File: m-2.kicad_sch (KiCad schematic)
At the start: 46 parts, among them J5 1-2199230-6, J6 1-2199230-6, M1 M2_2280, M2 M2_2280, P1 2199230-6

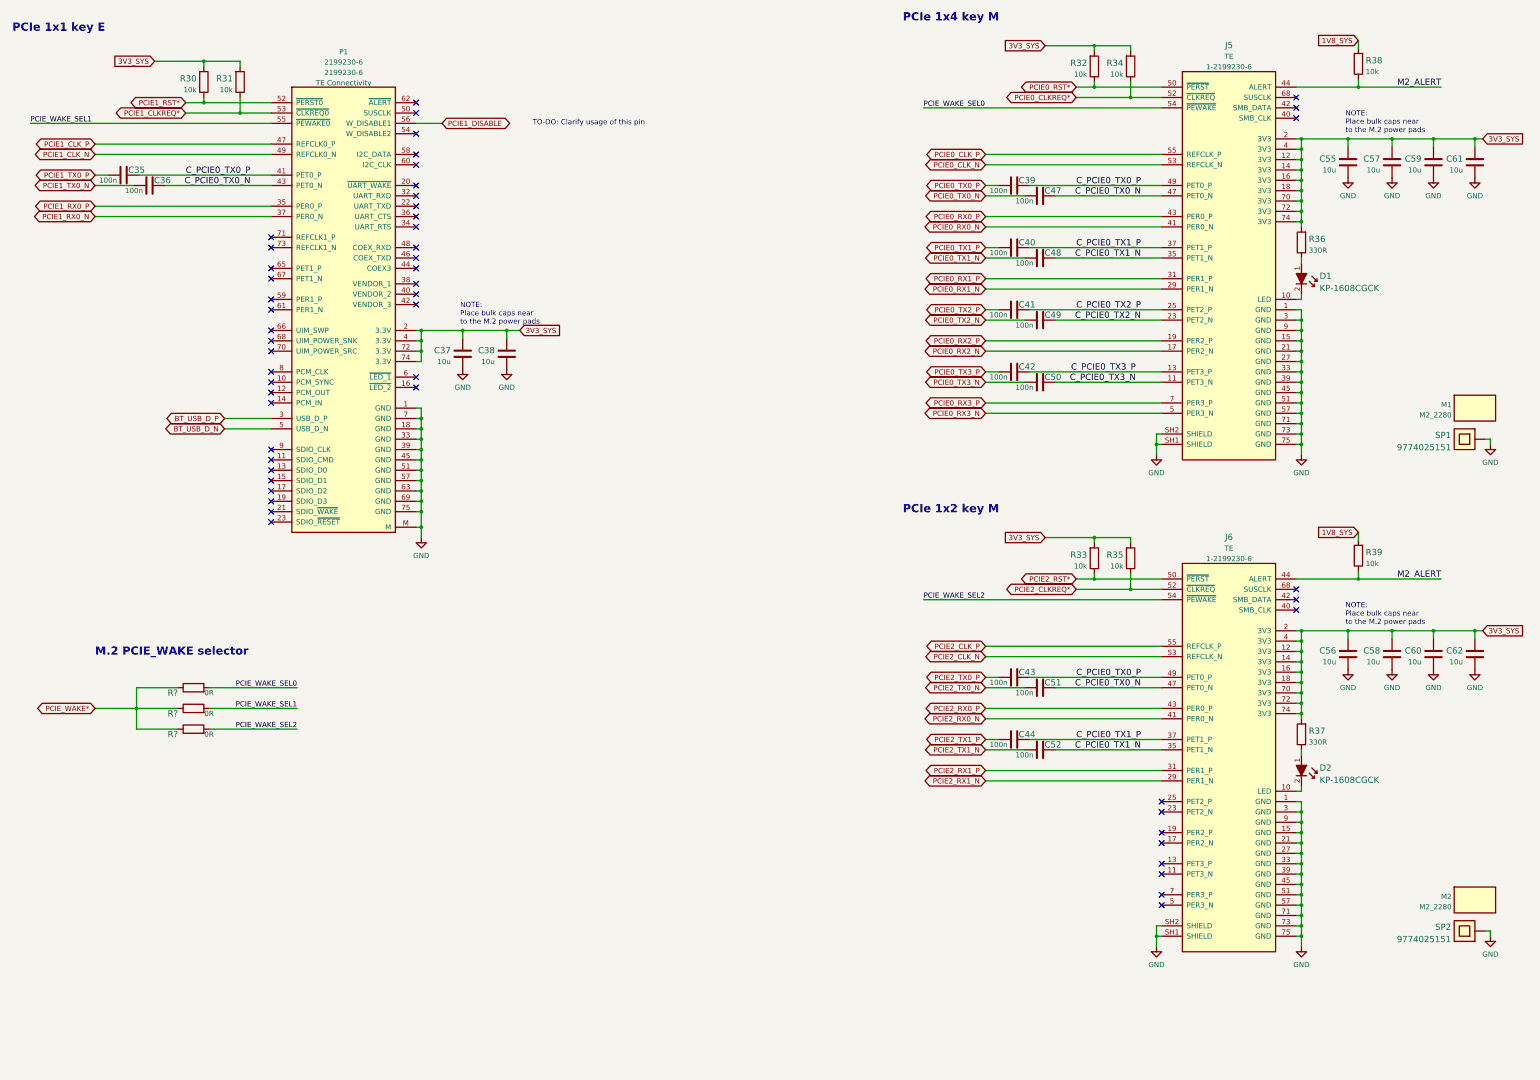
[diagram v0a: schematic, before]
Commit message: M.2 SCH: Add PCIe 0 Root Port / Endpoint mode switching circuitry
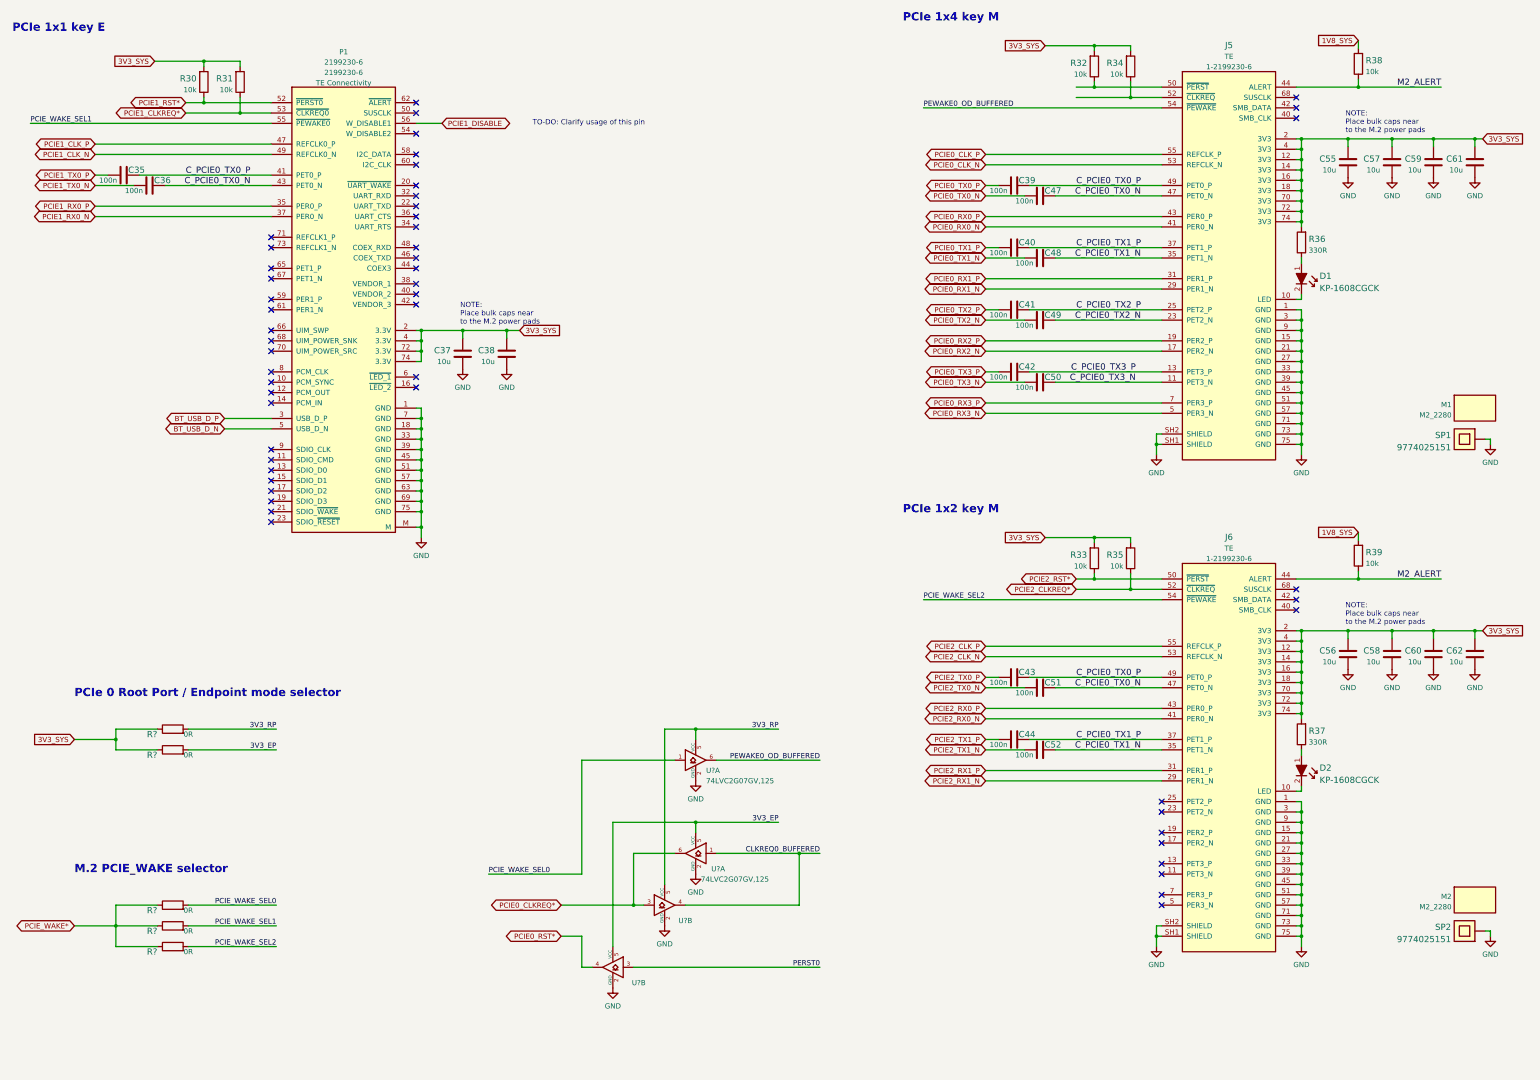
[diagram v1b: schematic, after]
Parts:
- added R? (x2): R_0R_0402, antmicro-footprints:0402-res, symbol antmicroResistors0402:R_0R_0402
- added U? (x4): 74LVC2G07GV,125, antmicro-footprints:SC-74, symbol antmicroLogicBuffersDriversReceiversTransceivers:74LVC2G07GV,125
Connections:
- net 3V3_SYS: now also R?.1, R?.1
- net GND: now also U?.2 (GND), U?.2 (GND), U?.2 (GND), U?.2 (GND)
- net PCIE0_CLKREQ*: now also U?.3, U?.6; no longer J5.52 (~{CLKREQ}), R34.1
- net PCIE0_RST*: now also U?.4; no longer J5.50 (~{PERST}), R32.1
- net PCIE_WAKE_SEL0: now also U?.1; no longer J5.54 (~{PEWAKE})
- new net: J5.52 (~{CLKREQ}), R34.1
- new net: J5.50 (~{PERST}), R32.1
- new net 3V3_EP: R?.2, U?.5 (VCC), U?.5 (VCC)
- new net 3V3_RP: R?.2, U?.5 (VCC), U?.5 (VCC)
- new net CLKREQ0_BUFFERED: U?.1, U?.4
- new net PERST0: U?.3
- new net PEWAKE0_OD_BUFFERED: J5.54 (~{PEWAKE}), U?.6
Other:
- note added: "PCIe 0 Root Port / Endpoint mode selector"
- moved on the sheet: R?

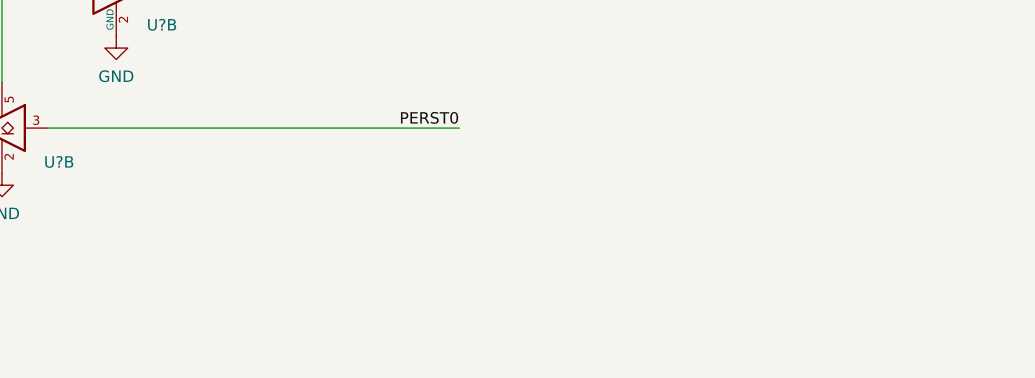
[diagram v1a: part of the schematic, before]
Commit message: M.2 SCH: Add note about PCIe 0 role switching
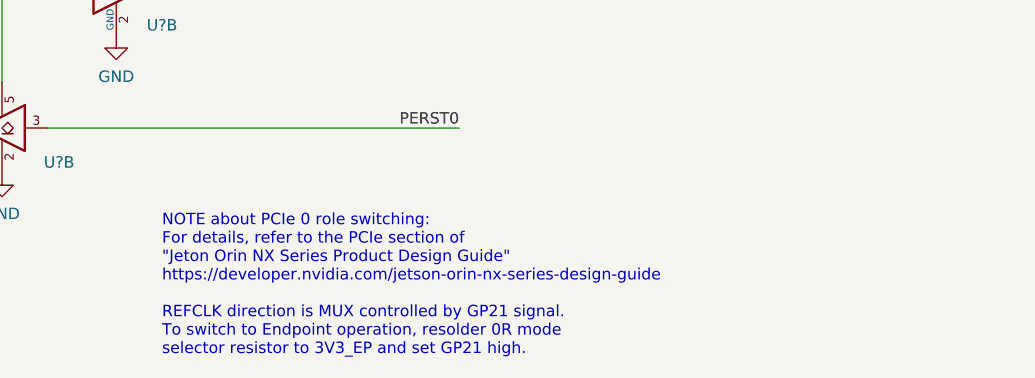
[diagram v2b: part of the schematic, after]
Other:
- note added: "NOTE about PCIe 0 role switching: For details, refer to the PCIe section of "Jeton Orin NX Series Product Design Guide" https://developer.nvidia.com/jetson-orin-nx-series-design-guide REFCLK direction is MUX controlled by GP21 signal. To switch to Endpoint operation, resolder 0R mode selector resistor to 3V3_EP and set GP21 high."
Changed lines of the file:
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@@
     (effects (font (size 2.0066 2.0066) (thickness 0.4013) bold) (justify left bottom))
+  )
+  (text "NOTE about PCIe 0 role switching:\nFor details, refer to the PCIe section of \n\"Jeton Orin NX Series Product Design Guide\"\nhttps://developer.nvidia.com/jetson-orin-nx-series-design-guide\n\nREFCLK direction is MUX controlled by GP21 signal.\nTo switch to Endpoint operation, resolder 0R mode\nselector resistor to 3V3_EP and set GP21 high."
+    (at 195.58 276.86 0)
+    (effects (font (size 1.27 1.27)) (justify left bottom))
   )
   (text "M.2 PCIE_WAKE selector" (at 45.72 228.6 0)

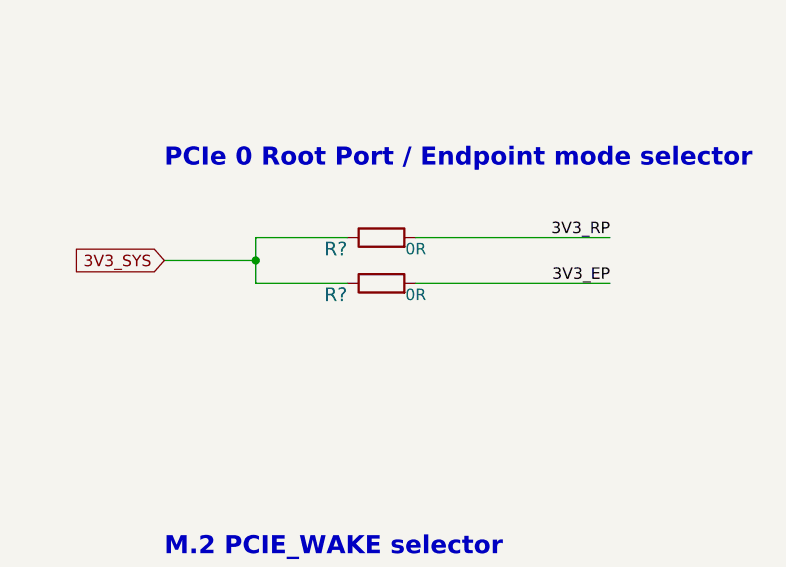
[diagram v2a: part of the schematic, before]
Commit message: M.2 SCH: Set PCIe 0 default role as Root Port by marking 3V3_EP resistor as DNP
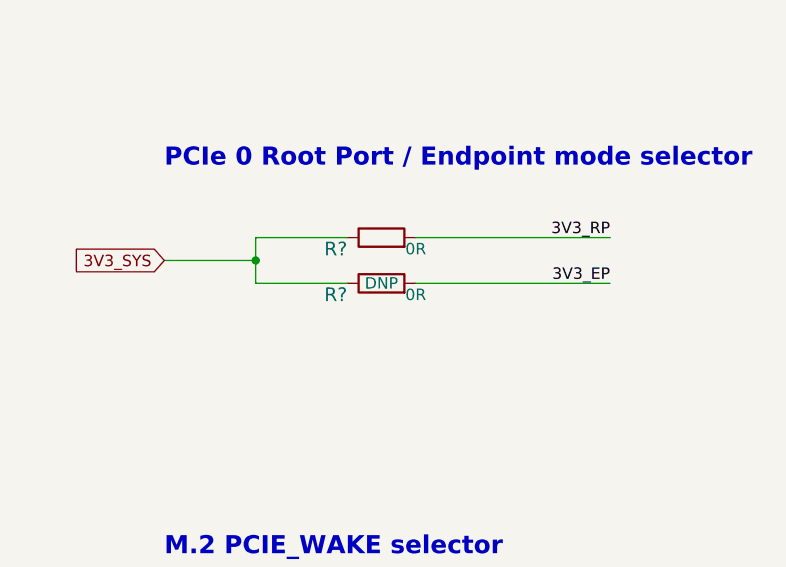
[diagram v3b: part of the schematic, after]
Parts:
- R?: DNP (none) -> DNP
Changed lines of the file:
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@@
     )
     (property "Val" "0R" (id 6) (at 73.66 199.39 0))
+    (property "DNP" "DNP" (id 7) (at 69.85 198.12 0))
     (pin "1")
     (pin "2")

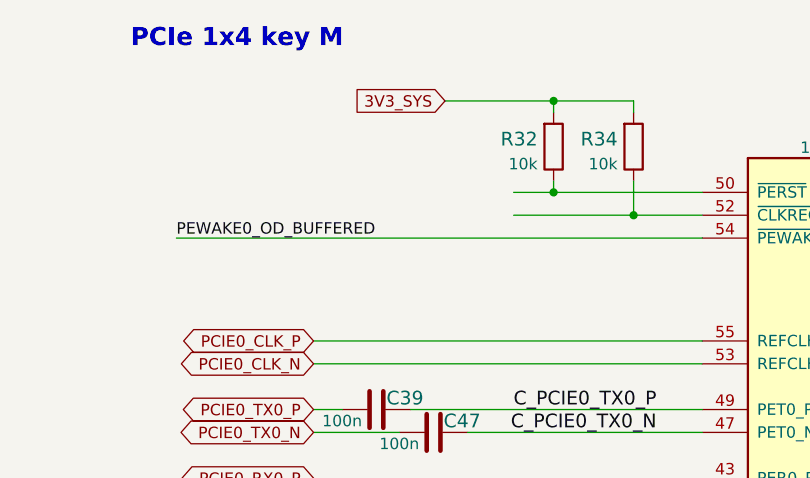
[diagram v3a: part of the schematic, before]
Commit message: M.2 SCH: Add missing internal labels for PCIe 0 control signals
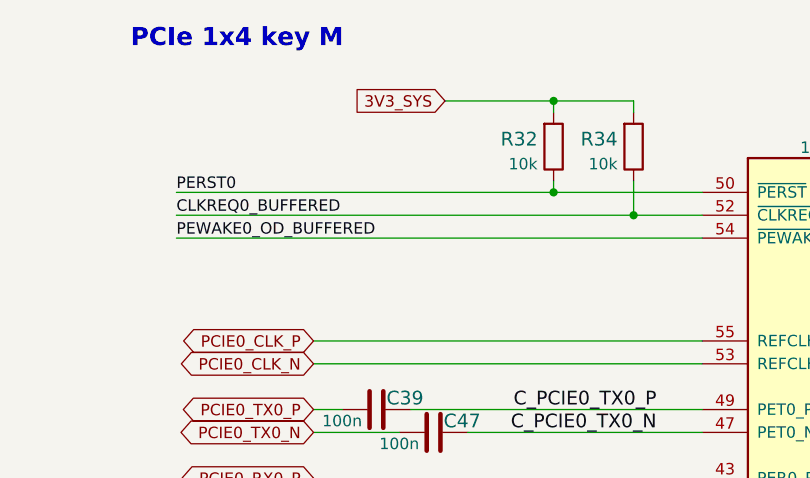
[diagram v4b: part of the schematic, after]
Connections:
- net CLKREQ0_BUFFERED: now also J5.52 (~{CLKREQ}), R34.1
- net PERST0: now also J5.50 (~{PERST}), R32.1
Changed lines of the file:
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@@
     (stroke (width 0) (type default) (color 0 0 0 0))
   )
-  (wire (pts (xy 291.465 38.1) (xy 304.8 38.1))
+  (wire (pts (xy 254 38.1) (xy 304.8 38.1))
     (stroke (width 0) (type default) (color 0 0 0 0))
   )
@@
     (stroke (width 0) (type default) (color 0 0 0 0))
   )
-  (wire (pts (xy 291.465 35.56) (xy 295.91 35.56))
+  (wire (pts (xy 254 35.56) (xy 295.91 35.56))
     (stroke (width 0) (type default) (color 0 0 0 0))
   )
@@
     (effects (font (size 1.524 1.524)) (justify right bottom))
   )
+  (label "CLKREQ0_BUFFERED" (at 254 38.1 0)
+    (effects (font (size 1.27 1.27)) (justify left bottom))
+  )
   (label "PEWAKE0_OD_BUFFERED" (at 254 40.64 0)
     (effects (font (size 1.27 1.27)) (justify left bottom))
@@
     (effects (font (size 1.524 1.524)) (justify right bottom))
   )
+  (label "PERST0" (at 254 35.56 0)
+    (effects (font (size 1.27 1.27)) (justify left bottom))
+  )
   (label "C_PCIE0_TX1_N" (at 307.34 77.47 180)

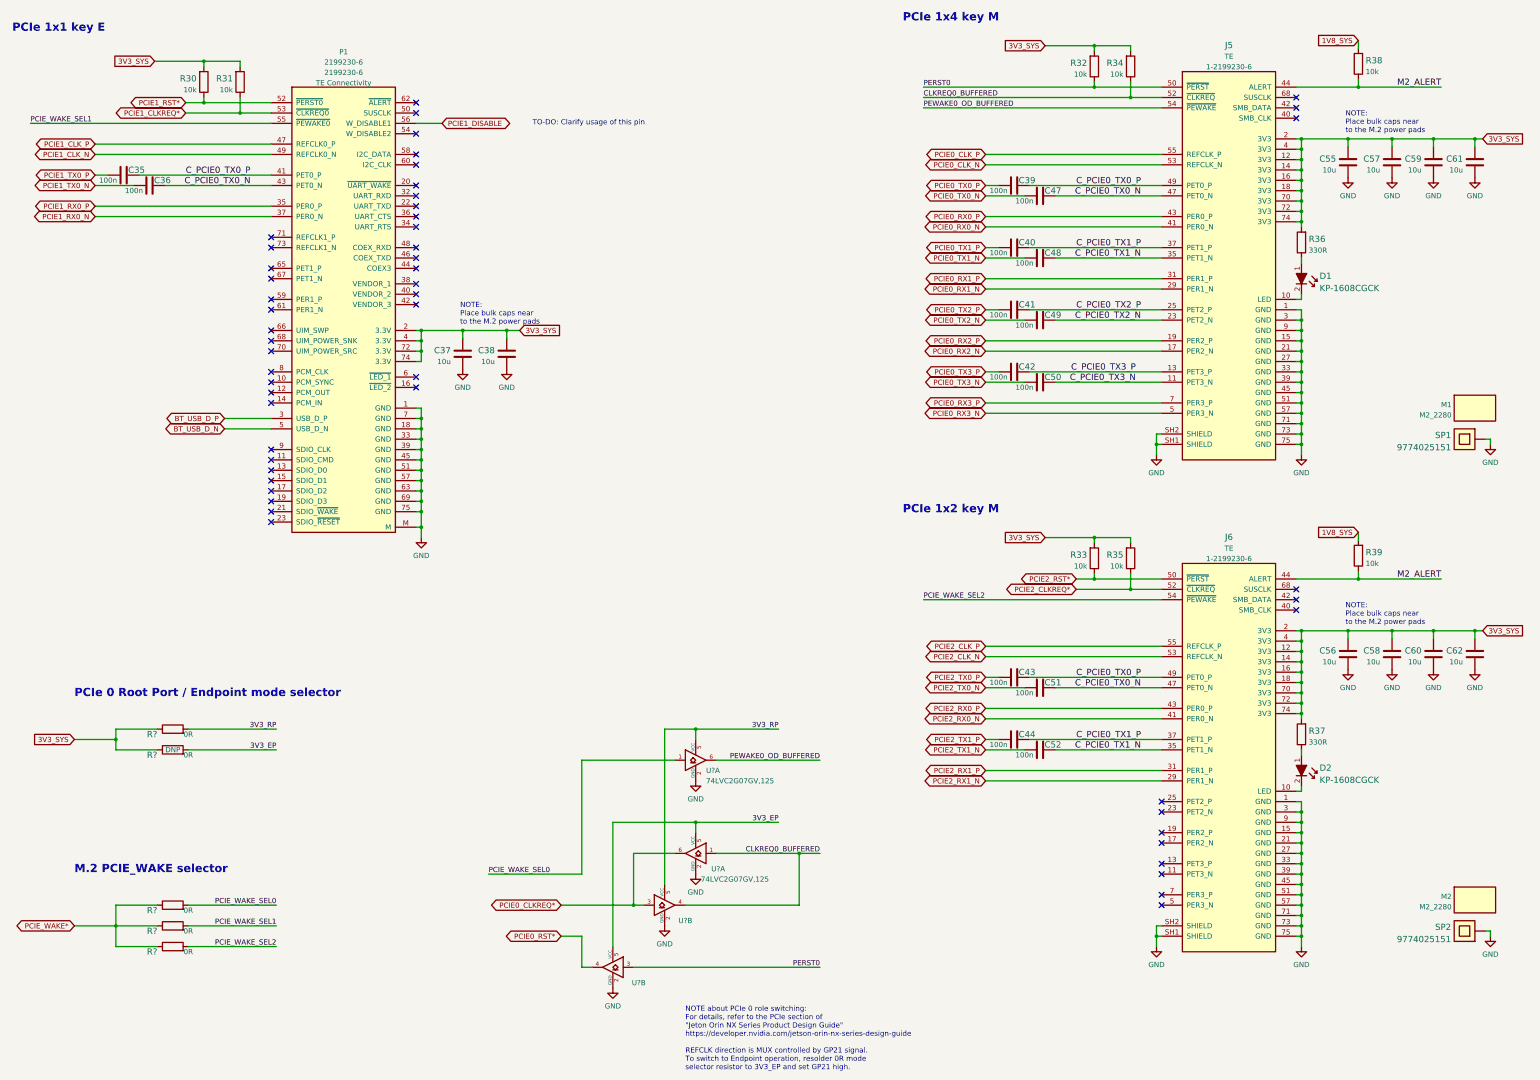
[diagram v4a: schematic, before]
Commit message: Added soft power button and annotated schematic
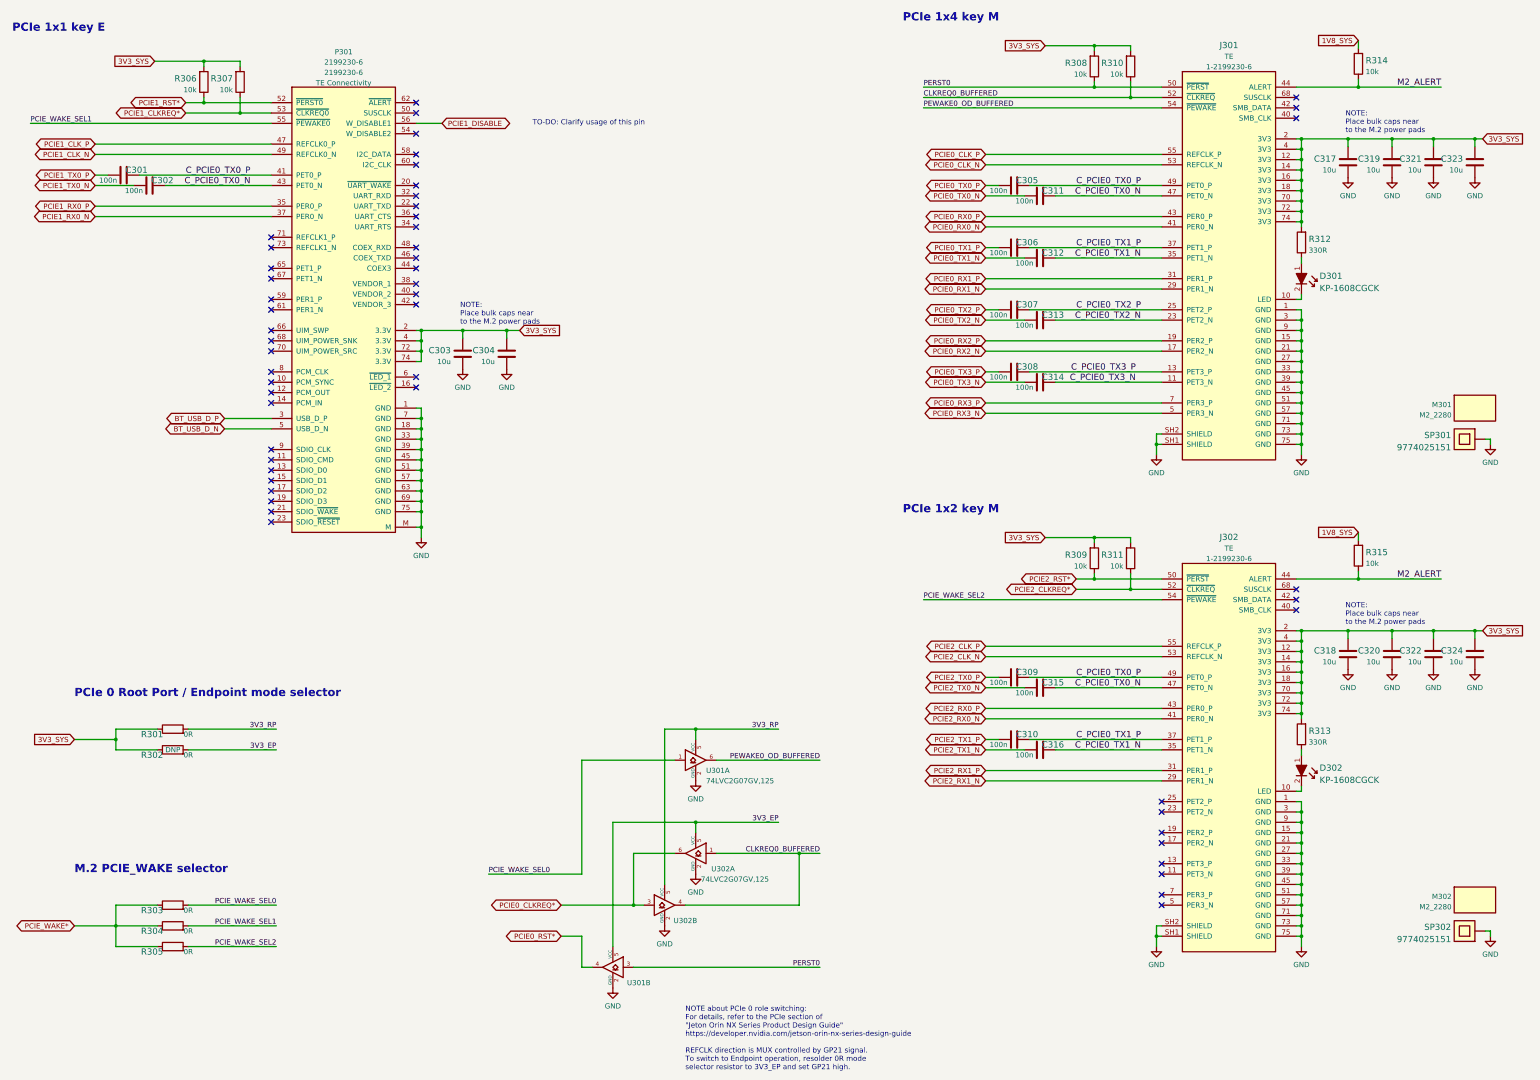
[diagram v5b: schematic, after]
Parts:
- gave numbers to parts that had none: 7
- renumbered C35 to C301, C36 to C302, C37 to C303, C38 to C304, C39 to C305, C40 to C306, C41 to C307, C42 to C308, C43 to C309, C44 to C310, C47 to C311, C48 to C312, C49 to C313, C50 to C314, C51 to C315, C52 to C316, C55 to C317, C56 to C318, C57 to C319, C58 to C320, C59 to C321, C60 to C322, C61 to C323, C62 to C324, D1 to D301, D2 to D302, J5 to J301, J6 to J302, M1 to M301, M2 to M302, P1 to P301, R30 to R306, R31 to R307, R32 to R308, R33 to R309, R34 to R310, R35 to R311, R36 to R312, R37 to R313, R38 to R314, R39 to R315, SP1 to SP301, SP2 to SP302
